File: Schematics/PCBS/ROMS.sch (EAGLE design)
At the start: 12 parts, among them IC1 ATMEGA328P-AU, M1 WIRELESS-NRF24L01-PA-EXT, Y1 16MHz

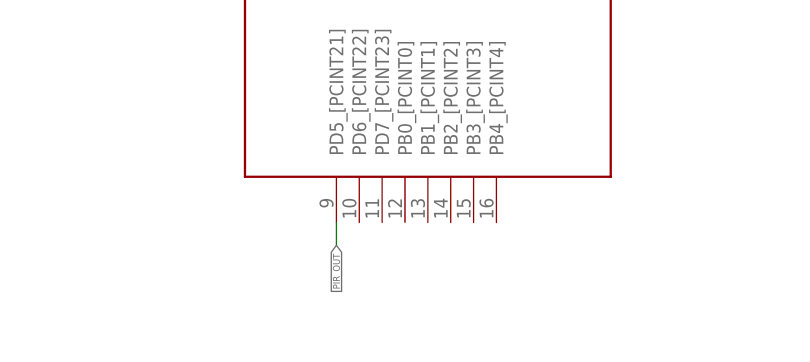
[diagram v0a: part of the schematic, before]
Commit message: added missing LED PCB link
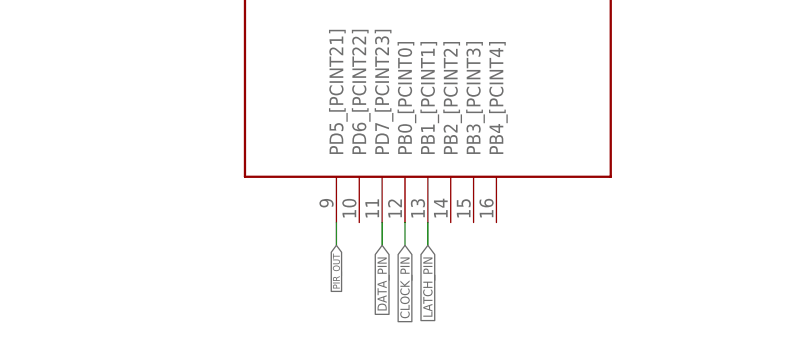
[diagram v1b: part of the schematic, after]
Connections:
- net CLOCK_PIN: now also IC1.PB0_[PCINT0]
- net DATA_PIN: now also IC1.PD7_[PCINT23]
- net LATCH_PIN: now also IC1.PB1_[PCINT1]
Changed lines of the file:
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@@
 <label x="-7.62" y="154.94" size="0.762" layer="95" xref="yes"/>
+</segment>
+<segment>
+<pinref part="IC1" gate="G$1" pin="PB1_[PCINT1]"/>
+<wire x1="76.2" y1="2.54" x2="76.2" y2="0" width="0.1524" layer="91"/>
+<label x="76.2" y="0" size="1.016" layer="95" rot="R270" xref="yes"/>
 </segment>
 </net>
@@
 <label x="-7.62" y="157.48" size="0.762" layer="95" xref="yes"/>
 </segment>
+<segment>
+<pinref part="IC1" gate="G$1" pin="PB0_[PCINT0]"/>
+<wire x1="73.66" y1="2.54" x2="73.66" y2="0" width="0.1524" layer="91"/>
+<label x="73.66" y="0" size="1.016" layer="95" rot="R270" xref="yes"/>
+</segment>
 </net>
 <net name="DATA_PIN" class="0">
@@
 <label x="-7.62" y="160.02" size="0.762" layer="95" xref="yes"/>
 </segment>
+<segment>
+<pinref part="IC1" gate="G$1" pin="PD7_[PCINT23]"/>
+<wire x1="71.12" y1="2.54" x2="71.12" y2="0" width="0.1524" layer="91"/>
+<label x="71.12" y="0" size="1.016" layer="95" rot="R270" xref="yes"/>
+</segment>
 </net>

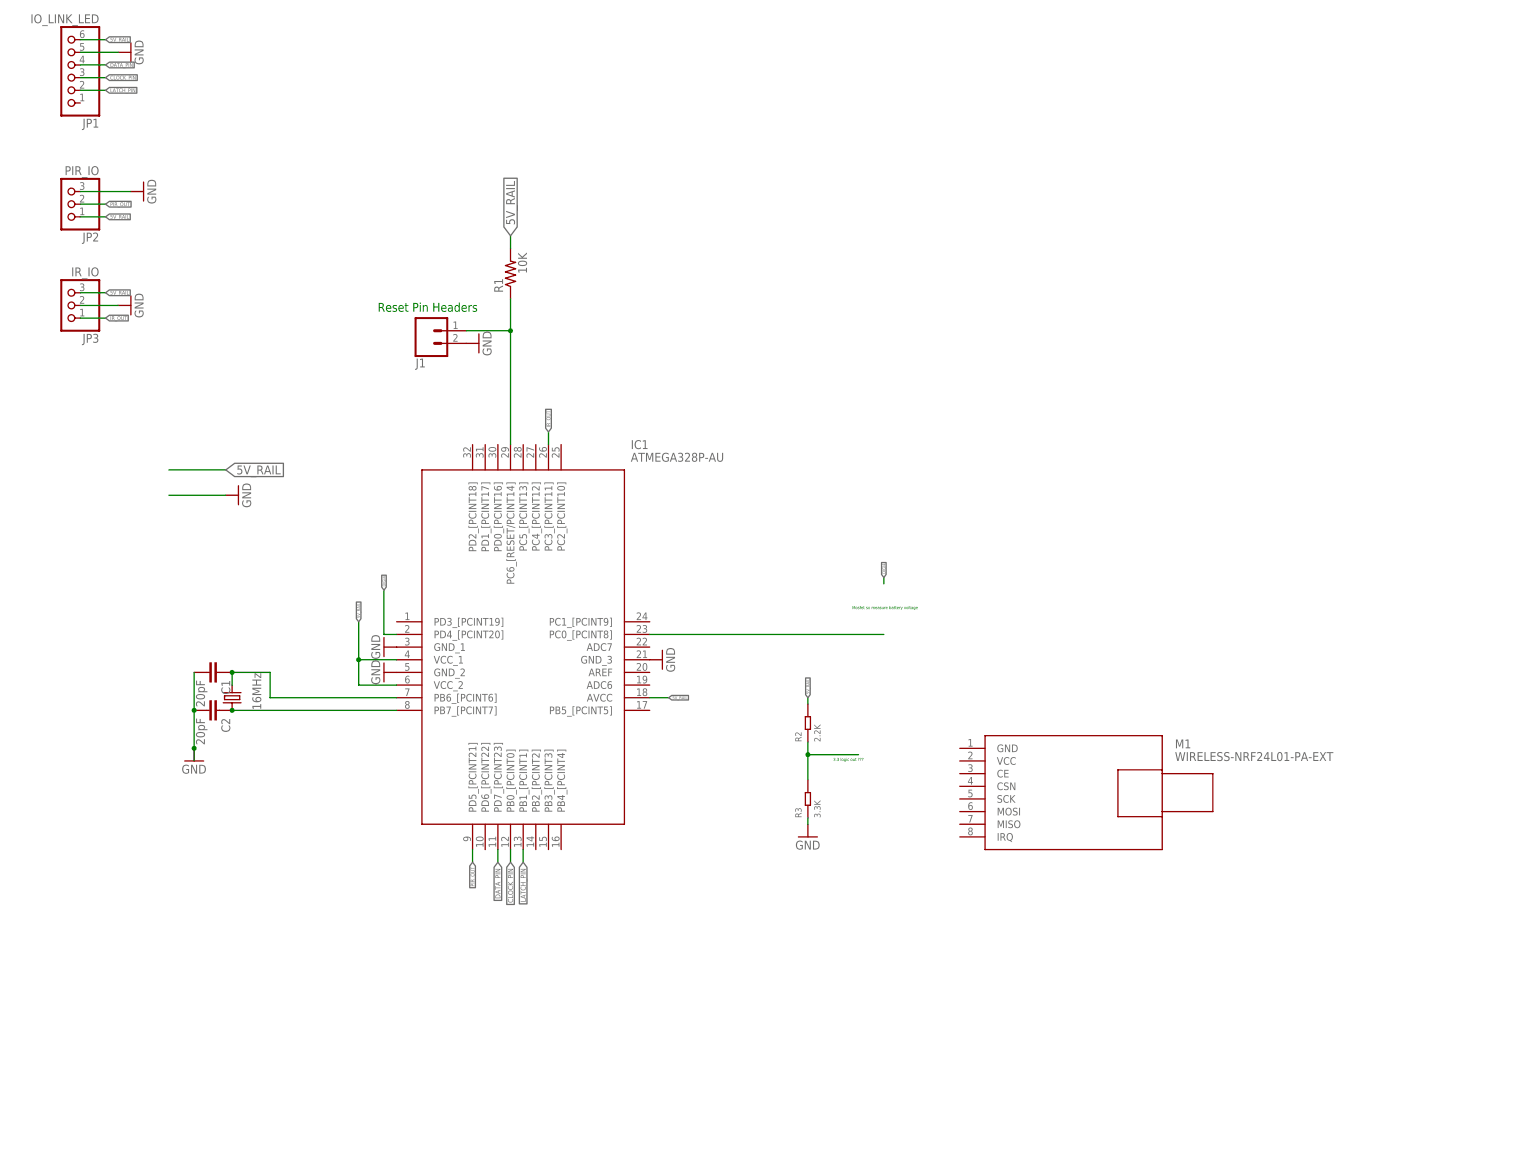
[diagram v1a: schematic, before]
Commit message: added volage divider for NRF24
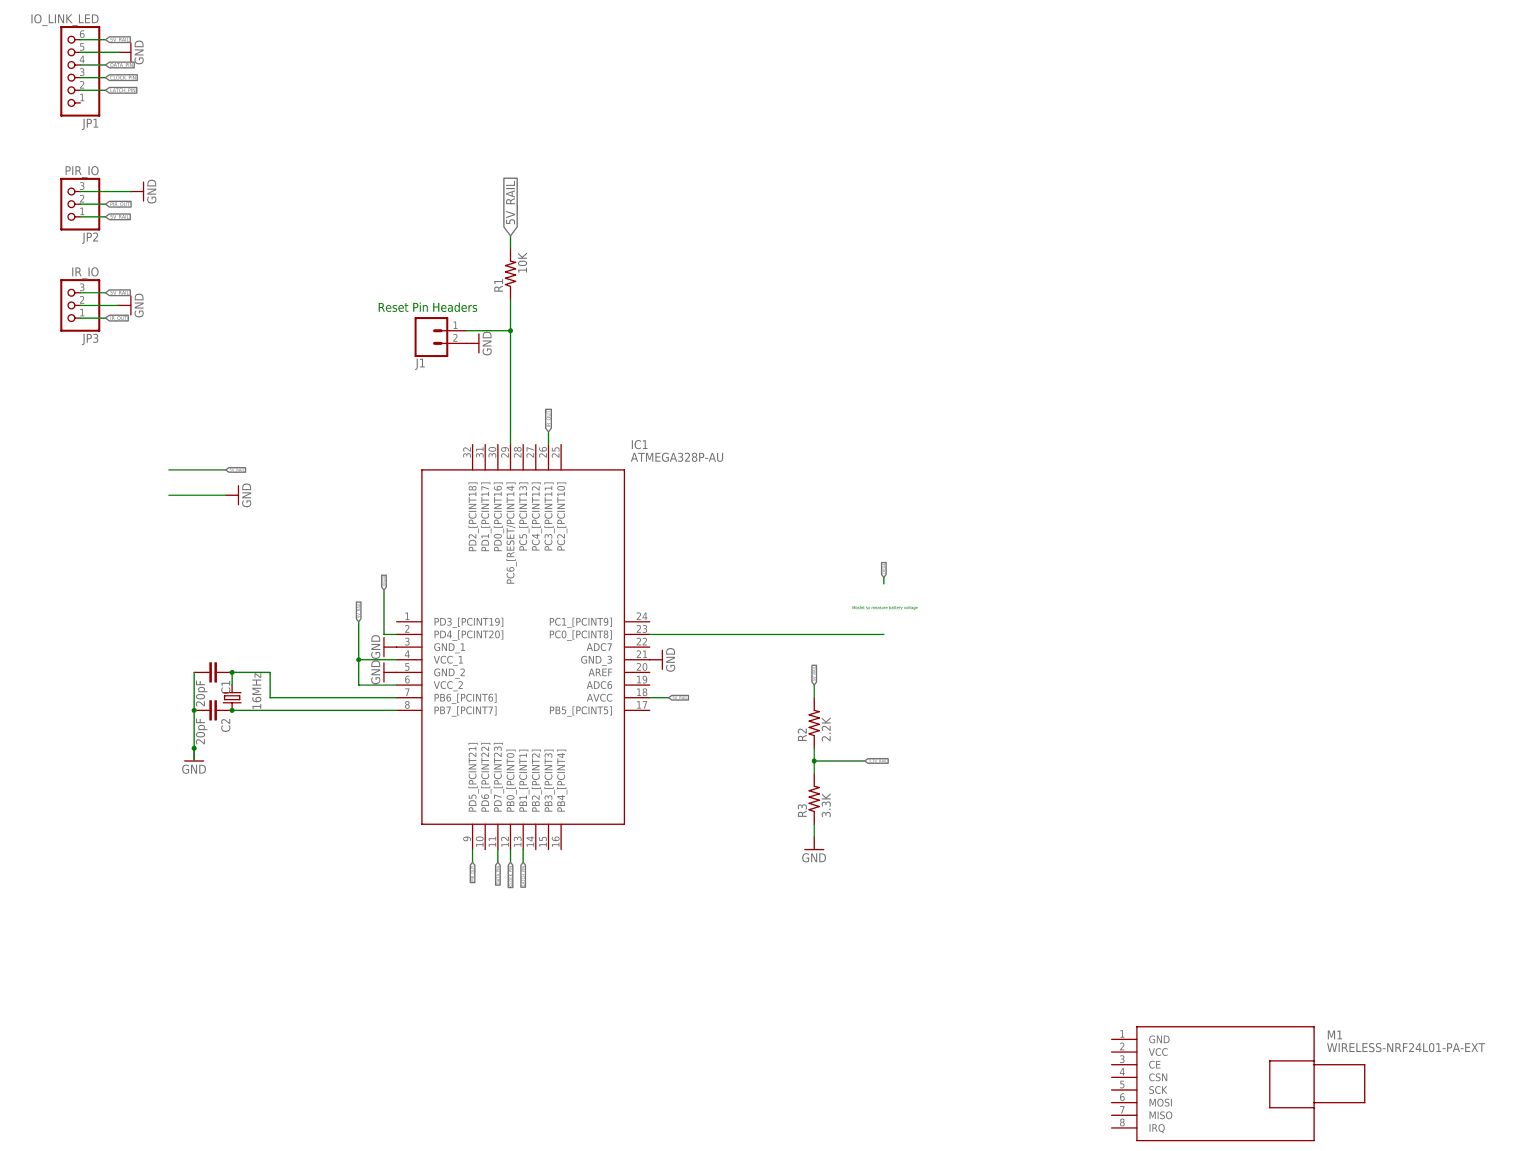
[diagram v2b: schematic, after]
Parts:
- R2: device Seeed-Resistor-2016:DIP-RES-2.2K-5%-1/4W(PR-D2.3XL6.5MM) -> adafruit:FLIPFLOP-RES
- R3: device Seeed-Resistor-2016:DIP-RES-3.3K-5%-1/4W(PR-D2.3XL6.5MM) -> adafruit:FLIPFLOP-RES
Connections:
- net N$5 renamed 3.3V_RAIL
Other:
- note removed: "3.3 logic out ???"
- moved on the sheet: M1
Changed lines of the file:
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@@
 <part name="GND6" library="supply1" library_urn="urn:adsk.eagle:library:371" deviceset="GND" device=""/>
 <part name="M1" library="diy-modules" deviceset="WIRELESS-NRF24L01-PA-EXT" device=""/>
-<part name="R2" library="Seeed-Resistor-2016" deviceset="DIP-RES-2.2K-5%-1/4W(PR-D2.3XL6.5MM)" device="" value="2.2K"/>
-<part name="R3" library="Seeed-Resistor-2016" deviceset="DIP-RES-3.3K-5%-1/4W(PR-D2.3XL6.5MM)" device="" value="3.3K"/>
 <part name="GND7" library="supply1" library_urn="urn:adsk.eagle:library:371" deviceset="GND" device=""/>
 <part name="JP1" library="adafruit" library_urn="urn:adsk.eagle:library:420" deviceset="PINHD-1X6" device="" package3d_urn="urn:adsk.eagle:package:6240711/1" value="IO_LINK_LED"/>
@@
 <part name="GND9" library="supply1" library_urn="urn:adsk.eagle:library:371" deviceset="GND" device=""/>
 <part name="GND10" library="supply1" library_urn="urn:adsk.eagle:library:371" deviceset="GND" device=""/>
+<part name="R2" library="adafruit" library_urn="urn:adsk.eagle:library:420" deviceset="FLIPFLOP-RES" device="" package3d_urn="urn:adsk.eagle:package:6240726/1" value="2.2K"/>
+<part name="R3" library="adafruit" library_urn="urn:adsk.eagle:library:420" deviceset="FLIPFLOP-RES" device="" package3d_urn="urn:adsk.eagle:package:6240726/1" value="3.3K"/>
 </parts>
 <sheets>
@@
 <text x="46.99" y="110.49" size="1.778" layer="91">Reset Pin Headers</text>
 <text x="142.24" y="50.8" size="0.6096" layer="91">Mosfet so measure battery voltage</text>
-<text x="138.43" y="20.32" size="0.6096" layer="91">3.3 logic out ???</text>
 </plain>
 <instances>
@@
 <attribute name="VALUE" x="69.85" y="101.6" size="1.778" layer="96" rot="R90"/>
 </instance>
-<instance part="M1" gate="G$1" x="186.69" y="12.7" smashed="yes">
-<attribute name="NAME" x="207.01" y="22.86" size="1.778" layer="95"/>
-<attribute name="VALUE" x="207.01" y="20.32" size="1.778" layer="96"/>
-</instance>
-<instance part="R2" gate="G$1" x="133.35" y="27.94" smashed="yes" rot="R90">
-<attribute name="NAME" x="132.08" y="24.13" size="1.27" layer="95" ratio="10" rot="R90"/>
-<attribute name="VALUE" x="135.89" y="24.13" size="1.27" layer="96" ratio="10" rot="R90"/>
-</instance>
-<instance part="R3" gate="G$1" x="133.35" y="12.7" smashed="yes" rot="R90">
-<attribute name="NAME" x="132.08" y="8.89" size="1.27" layer="95" ratio="10" rot="R90"/>
-<attribute name="VALUE" x="135.89" y="8.89" size="1.27" layer="96" ratio="10" rot="R90"/>
-</instance>
-<instance part="GND7" gate="1" x="133.35" y="5.08" smashed="yes">
-<attribute name="VALUE" x="130.81" y="2.54" size="1.778" layer="96"/>
+<instance part="M1" gate="G$1" x="217.17" y="-45.72" smashed="yes">
+<attribute name="NAME" x="237.49" y="-35.56" size="1.778" layer="95"/>
+<attribute name="VALUE" x="237.49" y="-38.1" size="1.778" layer="96"/>
+</instance>
+<instance part="GND7" gate="1" x="134.62" y="2.54" smashed="yes">
+<attribute name="VALUE" x="132.08" y="0" size="1.778" layer="96"/>
 </instance>
 <instance part="JP1" gate="A" x="-15.24" y="160.02" smashed="yes" rot="R180">
@@
 <instance part="GND10" gate="1" x="-2.54" y="162.56" smashed="yes" rot="R90">
 <attribute name="VALUE" x="0" y="160.02" size="1.778" layer="96" rot="R90"/>
+</instance>
+<instance part="R2" gate="G$1" x="134.62" y="27.94" smashed="yes" rot="R90">
+<attribute name="NAME" x="133.1214" y="24.13" size="1.778" layer="95" rot="R90"/>
+<attribute name="VALUE" x="137.922" y="24.13" size="1.778" layer="96" rot="R90"/>
+</instance>
+<instance part="R3" gate="G$1" x="134.62" y="12.7" smashed="yes" rot="R90">
+<attribute name="NAME" x="133.1214" y="8.89" size="1.778" layer="95" rot="R90"/>
+<attribute name="VALUE" x="137.922" y="8.89" size="1.778" layer="96" rot="R90"/>
 </instance>
 </instances>
@@
 </segment>
 <segment>
+<pinref part="GND7" gate="1" pin="GND"/>
 <pinref part="R3" gate="G$1" pin="1"/>
-<pinref part="GND7" gate="1" pin="GND"/>
-<wire x1="133.35" y1="8.89" x2="133.35" y2="7.62" width="0.1524" layer="91"/>
+<wire x1="134.62" y1="5.08" x2="134.62" y2="7.62" width="0.1524" layer="91"/>
 </segment>
 <segment>
@@
 </segment>
 </net>
-<net name="N$5" class="0">
-<segment>
-<pinref part="R3" gate="G$1" pin="2"/>
-<pinref part="R2" gate="G$1" pin="1"/>
-<wire x1="133.35" y1="16.51" x2="133.35" y2="21.59" width="0.1524" layer="91"/>
-<wire x1="133.35" y1="21.59" x2="133.35" y2="24.13" width="0.1524" layer="91"/>
-<wire x1="133.35" y1="21.59" x2="143.51" y2="21.59" width="0.1524" layer="91"/>
-<junction x="133.35" y="21.59"/>
-</segment>
-</net>
 <net name="LATCH_PIN" class="0">
 <segment>
@@
 <pinref part="IC1" gate="G$1" pin="PB1_[PCINT1]"/>
 <wire x1="76.2" y1="2.54" x2="76.2" y2="0" width="0.1524" layer="91"/>
-<label x="76.2" y="0" size="1.016" layer="95" rot="R270" xref="yes"/>
+<label x="76.2" y="0" size="0.6096" layer="95" rot="R270" xref="yes"/>
 </segment>
 </net>
@@
 <pinref part="IC1" gate="G$1" pin="PB0_[PCINT0]"/>
 <wire x1="73.66" y1="2.54" x2="73.66" y2="0" width="0.1524" layer="91"/>
-<label x="73.66" y="0" size="1.016" layer="95" rot="R270" xref="yes"/>
+<label x="73.66" y="0" size="0.6096" layer="95" rot="R270" xref="yes"/>
 </segment>
 </net>
@@
 <pinref part="IC1" gate="G$1" pin="PD7_[PCINT23]"/>
 <wire x1="71.12" y1="2.54" x2="71.12" y2="0" width="0.1524" layer="91"/>
-<label x="71.12" y="0" size="1.016" layer="95" rot="R270" xref="yes"/>
+<label x="71.12" y="0" size="0.6096" layer="95" rot="R270" xref="yes"/>
 </segment>
 </net>
@@
 <pinref part="IC1" gate="G$1" pin="PD5_[PCINT21]"/>
 <wire x1="66.04" y1="2.54" x2="66.04" y2="0" width="0.1524" layer="91"/>
-<label x="66.04" y="0" size="0.762" layer="95" rot="R270" xref="yes"/>
+<label x="66.04" y="0" size="0.6096" layer="95" rot="R270" xref="yes"/>
 </segment>
 </net>
@@
 <segment>
 <wire x1="5.08" y1="78.74" x2="16.51" y2="78.74" width="0.1524" layer="91"/>
-<label x="16.51" y="78.74" size="1.778" layer="95" xref="yes"/>
+<label x="16.51" y="78.74" size="0.6096" layer="95" xref="yes"/>
 </segment>
 <segment>
@@
 </segment>
 <segment>
+<wire x1="134.62" y1="35.56" x2="134.62" y2="33.02" width="0.1524" layer="91"/>
+<label x="134.62" y="35.56" size="0.6096" layer="95" rot="R90" xref="yes"/>
 <pinref part="R2" gate="G$1" pin="2"/>
-<wire x1="133.35" y1="31.75" x2="133.35" y2="33.02" width="0.1524" layer="91"/>
-<label x="133.35" y="33.02" size="0.6096" layer="95" rot="R90" xref="yes"/>
 </segment>
 <segment>
@@
 </segment>
 </net>
+<net name="3.3V_RAIL" class="0">
+<segment>
+<pinref part="R3" gate="G$1" pin="2"/>
+<pinref part="R2" gate="G$1" pin="1"/>
+<wire x1="134.62" y1="22.86" x2="134.62" y2="20.32" width="0.1524" layer="91"/>
+<label x="144.78" y="20.32" size="0.6096" layer="95" xref="yes"/>
+<wire x1="134.62" y1="20.32" x2="134.62" y2="17.78" width="0.1524" layer="91"/>
+<wire x1="134.62" y1="20.32" x2="144.78" y2="20.32" width="0.1524" layer="91"/>
+<junction x="134.62" y="20.32"/>
+</segment>
+</net>
